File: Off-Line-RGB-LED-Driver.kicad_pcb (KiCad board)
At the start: 2 copper layers, 102 x 102 mm, 110 parts, among them J1 SolderWire_LED+, J2 SolderWire_LED-, J3 SolderWire_LED+, J4 SolderWire_LED-, J5 SolderWire_LED+, J6 SolderWire_LED-, J7 Conn_01x06_Pin, P1 Conn_WallPlug_Earth, Q1 IPN70R1K4P7S, Q2 IPN70R1K4P7S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

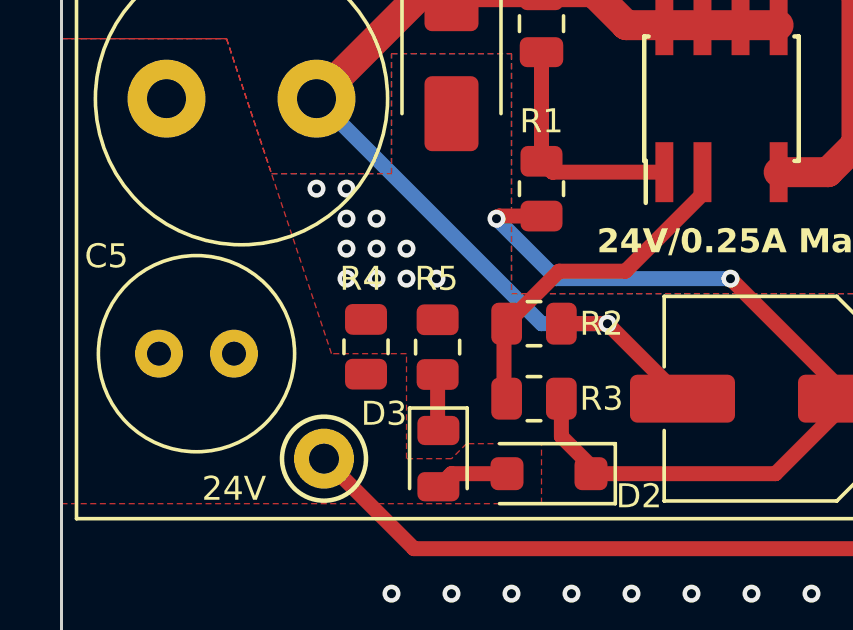
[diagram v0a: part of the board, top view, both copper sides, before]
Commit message: [A02] Edited R4, R5
R4 20k -> 10k since nothing else uses 20k
R5 10k -> 510k to reduce D3 LED brightness
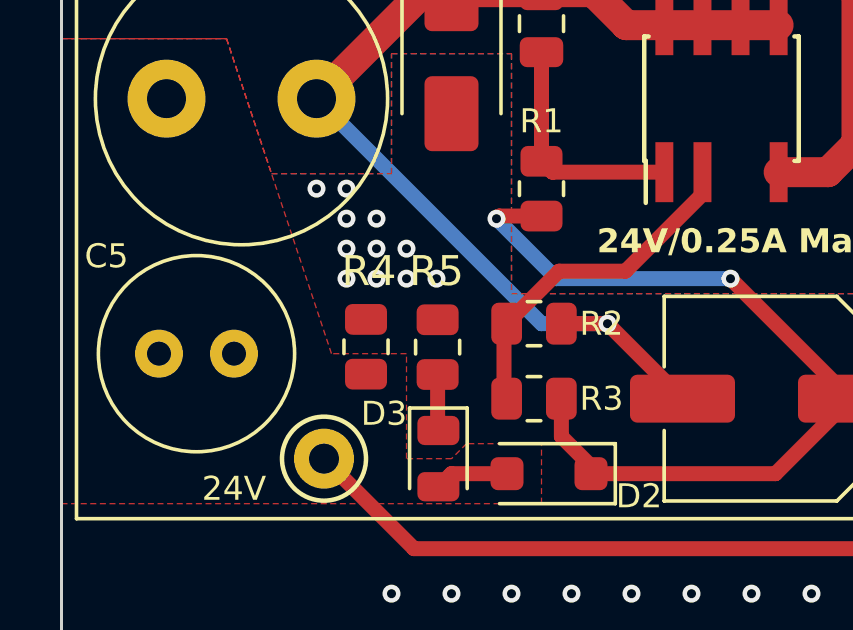
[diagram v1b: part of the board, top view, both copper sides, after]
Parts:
- R4: value 0805,20k -> 0805,10k
- R5: value 0805,10k -> 0805,510k
